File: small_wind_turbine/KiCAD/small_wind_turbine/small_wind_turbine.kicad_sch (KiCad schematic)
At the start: 17 parts

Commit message: wip schematic
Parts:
- added R? (x2): 2.5k, symbol Device:R
- added R?: 100, symbol Device:R
- added U? (x5): Opamp_Quad, symbol Device:Opamp_Quad
- added U?: AD8276, symbol Amplifier_Difference:AD8276
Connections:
- net GND1: now also U?.1 (REF), U?.11 (V-), U?.4 (V-), U?.9 (-)
- net OUTPUT_ISENSE_DOWNSTREAM: now reaches J?.1 (Pin_1), R?.2
- net OUTPUT_ISENSE_DOWNSTREAM: now also U?.5 (+)
- net RECTIFIER_VDD renamed OUTPUT_ISENSE_UPSTREAM
- net OUTPUT_ISENSE_UPSTREAM: now also U?.3 (+)
- new net: R?.1, R?.2, R?.2, U?.10 (+)
- new net: R?.1, U?.5 (SENSE), U?.6
- new net: U?.2 (-), U?.6 (-), U?.7
- new net: U?.1, U?.2 (-), U?.3 (+)
- new net: R?.2, U?.8
- new net +5V: U?.4 (V+), U?.7 (V+)
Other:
- moved on the sheet: U?

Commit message: finish current sensing feedback circuit
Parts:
- added C? (x3): C, symbol Device:C
- added R? (x3): R, symbol Device:R
- added U?: MCP3021, symbol just_energy_hub:MCP3021
- added U?: MCP4725xxx-xCH, Package_TO_SOT_SMD:SOT-23-6, symbol Analog_DAC:MCP4725xxx-xCH
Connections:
- net OUTPUT_ISENSE_DOWNSTREAM is gone; now on net BATTERY_POSITIVE: J?.1 (Pin_1), R?.2, U?.5 (+)
- net +5V: now also U?.1 (VDD), U?.3 (VDD)
- net GND1: now also C?.2, U?.2 (VSS), U?.2 (VSS)
- net at R?.1: now also U?.1 (VOUT)
- net UC2844_COMP: now reaches U?.1 (COMP)
- net UC2844_COMP: now also C?.1, C?.2
- net UC2844_FB: now reaches U?.2 (FB)
- net UC2844_FB: now also C?.2, R?.1, R?.2
- net UC2844_ISENSE: now reaches U?.3 (ISENSE)
- net UC2844_ISENSE: now also Q?.1 (D), R?.2
- net UC2844_RTCT: now reaches U?.4 (RT/CT)
- net UC2844_RTCT: now also C?.1, R?.2
- net UC2844_GATE_DRIVE: now reaches U?.6 (OUTPUT)
- net UC2844_GATE_DRIVE: now also Q?.2 (G)
- net UC2844_VREF: now reaches U?.8 (VREF)
- net UC2844_VREF: now also R?.1
- net BATTERY_NEGATIVE: now reaches C?.2, J?.2 (Pin_2), L?.1
- net BATTERY_POSITIVE: now reaches U?.12 (+)
- net at U?.13 (-): now also U?.14, U?.3 (AIN)
- net at R?.2, U?.8: now also R?.1
- new net: C?.1, R?.2
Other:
- moved on the sheet: C?, D?, J?, L?, Q?, R?, U?, U?A, U?B, U?C, U?E

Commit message: wip schematic
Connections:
- net GND: now also U?.5 (GND)
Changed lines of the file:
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@@
     (stroke (width 0) (type default) (color 0 0 0 0))
   )
-  (wire (pts (xy 41.91 195.58) (xy 41.91 201.93))
+  (wire (pts (xy 41.91 195.58) (xy 41.91 198.12))
     (stroke (width 0) (type default) (color 0 0 0 0))
   )
@@
   (label "UC2844_RTCT" (at 45.72 149.86 180)
     (effects (font (size 1.27 1.27)) (justify right bottom))
+  )
+  (label "RECTIFIER_GND" (at 68.58 149.86 0)
+    (effects (font (size 1.27 1.27)) (justify left bottom))
   )
   (label "OUTPUT_ISENSE_DOWNSTREAM" (at 121.92 71.12 0)
@@
     (pin "2")
   )
-  (symbol (lib_id "power:GND1") (at 41.91 201.93 0) (unit 1)
+  (symbol (lib_id "power:GND1") (at 41.91 198.12 0) (unit 1)
     (in_bom yes) (on_board yes) (fields_autoplaced)
-    (property "Reference" "#PWR?" (id 0) (at 41.91 208.28 0)
+    (property "Reference" "#PWR?" (id 0) (at 41.91 204.47 0)
       (effects (font (size 1.27 1.27)) hide)
     )
-    (property "Value" "GND1" (id 1) (at 41.91 207.01 0))
-    (property "Footprint" "" (id 2) (at 41.91 201.93 0)
+    (property "Value" "GND1" (id 1) (at 41.91 203.2 0))
+    (property "Footprint" "" (id 2) (at 41.91 198.12 0)
       (effects (font (size 1.27 1.27)) hide)
     )
-    (property "Datasheet" "" (id 3) (at 41.91 201.93 0)
+    (property "Datasheet" "" (id 3) (at 41.91 198.12 0)
       (effects (font (size 1.27 1.27)) hide)
     )

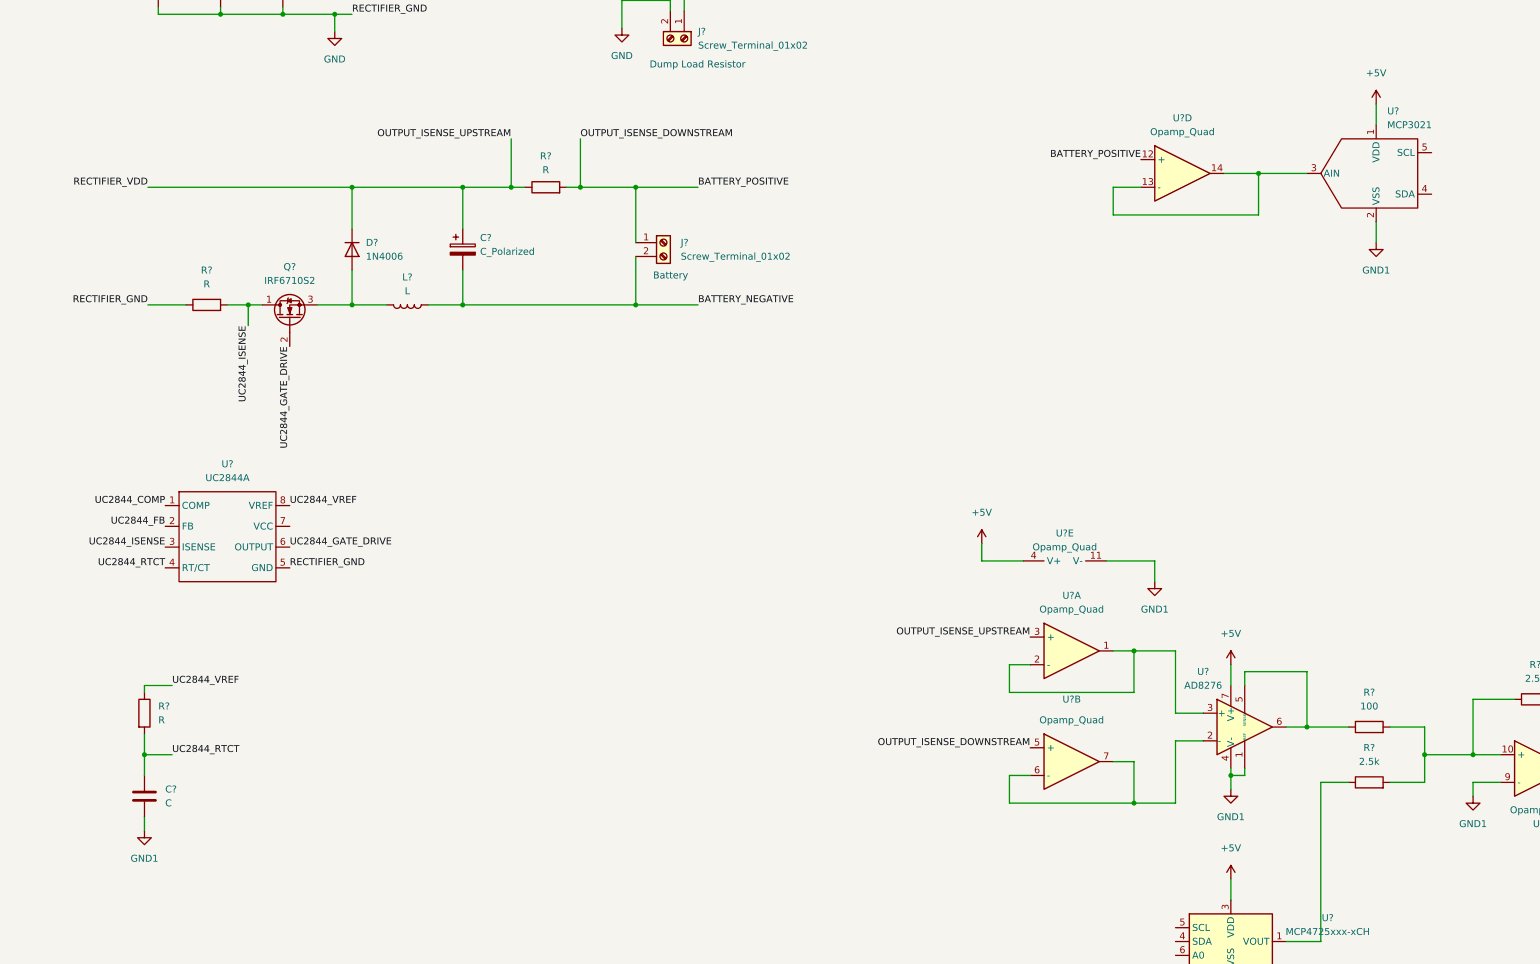
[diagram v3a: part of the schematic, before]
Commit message: add high side gate driver and connect common grounds
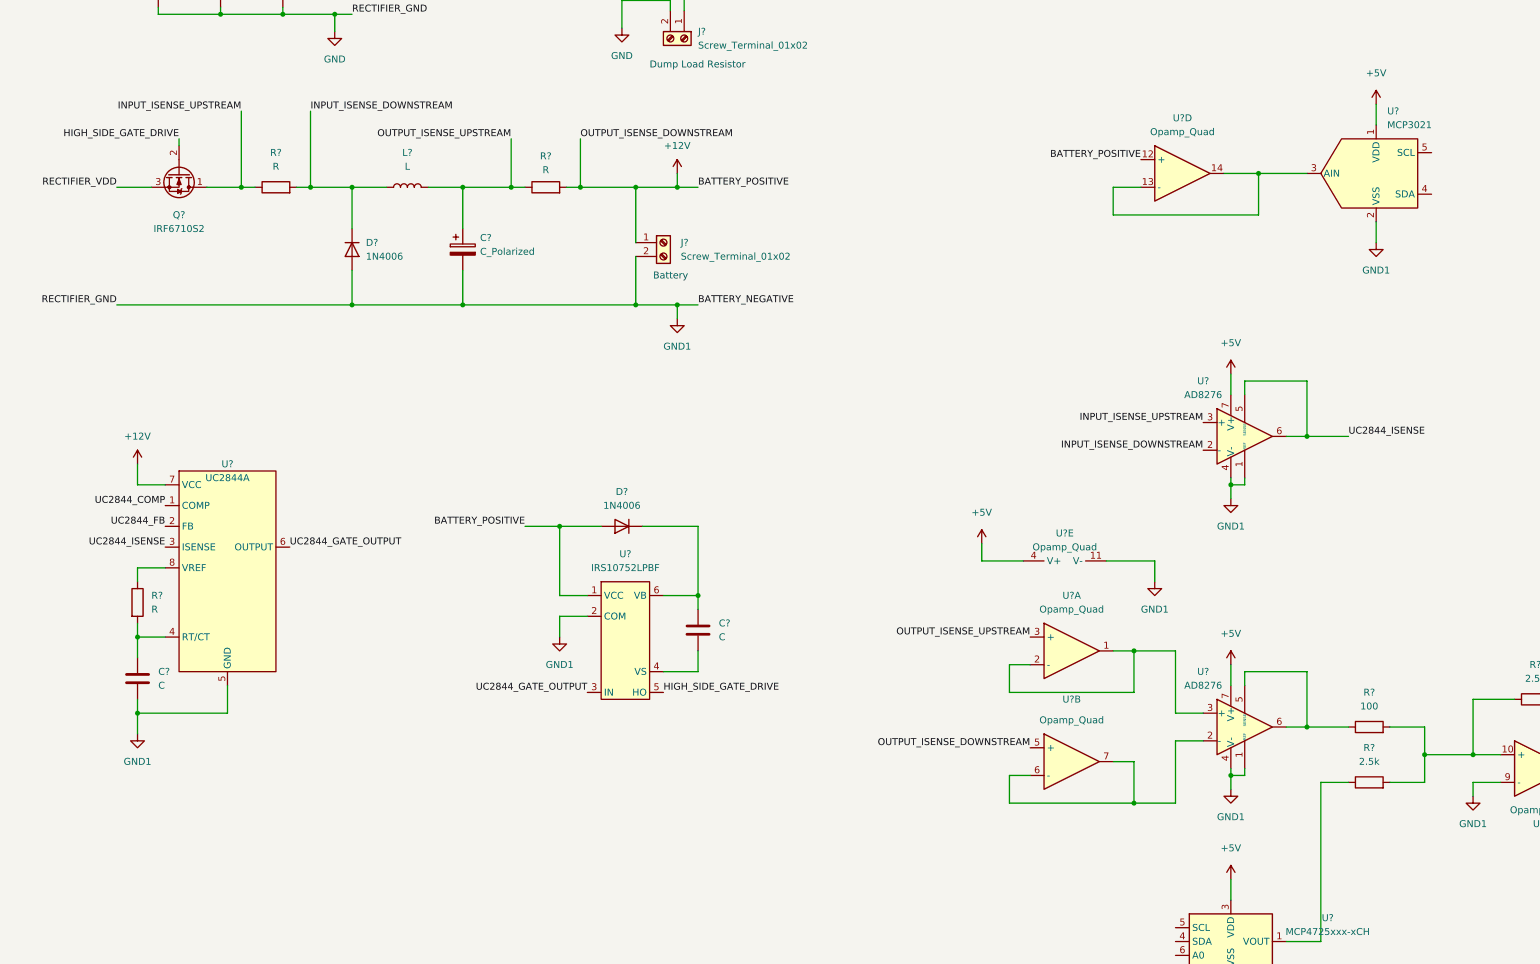
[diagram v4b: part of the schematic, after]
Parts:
- added C?: C, symbol Device:C
- added D?: 1N4006, Diode_THT:D_DO-41_SOD81_P10.16mm_Horizontal, symbol Diode:1N4006
- added U?: IRS10752LPBF, symbol just_energy_hub:IRS10752LPBF
- added U?: AD8276, symbol Amplifier_Difference:AD8276
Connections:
- net BATTERY_POSITIVE is gone; now on net +12V: J?.1 (Pin_1), R?.2, U?.12 (+), U?.5 (+)
- net GND1 is gone; now on net GND: C?.2, K?.A1, U?.1 (REF), U?.11 (V-), U?.2 (VSS), U?.2 (VSS), U?.4 (V-), U?.9 (-)
- net +5V: now also U?.7 (V+)
- net GND: now also C?.2, D?.2 (A), J?.2 (Pin_2), U?.1 (REF), U?.2 (COM), U?.4 (V-); no longer R?.1
- net OUTPUT_ISENSE_UPSTREAM: now also L?.2; no longer D?.1 (K), SW?.1 (A)
- net UC2844_ISENSE: now also U?.5 (SENSE), U?.6; no longer Q?.1 (D), R?.2
- net +12V: now reaches U?.7 (VCC)
- net +12V: now also D?.2 (A), U?.1 (VCC)
- removed net BATTERY_NEGATIVE: C?.2, J?.2 (Pin_2), L?.1
- net UC2844_GATE_DRIVE renamed HIGH_SIDE_GATE_DRIVE
- net HIGH_SIDE_GATE_DRIVE: now also U?.5 (HO); no longer U?.6 (OUTPUT)
- net UC2844_RTCT: no longer names the net of C?.1, R?.2, U?.4 (RT/CT)
- net UC2844_VREF: no longer names the net of R?.1, U?.8 (VREF)
- new net: C?.2, U?.4 (VS)
- new net: C?.1, D?.1 (K), U?.6 (VB)
- new net INPUT_ISENSE_DOWNSTREAM: D?.1 (K), L?.1, R?.2, U?.2 (-)
- new net INPUT_ISENSE_UPSTREAM: Q?.1 (D), R?.1, U?.3 (+)
- new net RECTIFIER_VDD: Q?.3 (S), SW?.1 (A)
- new net UC2844_GATE_OUTPUT: U?.3 (IN), U?.6 (OUTPUT)
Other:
- moved on the sheet: C?, L?, Q?, R?

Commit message: wip schematic. Replace inverting adder with non-inverting adder. Postulate on replacing Isense resistor for UC2844
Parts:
- added D?: D_Zener, symbol Device:D_Zener
- added J?: Screw_Terminal_01x03, symbol Connector:Screw_Terminal_01x03
- added R?: 100, symbol Device:R
- added R? (x2): 4.7k, symbol Device:R
- added R?: 62k, symbol Device:R
- added R?: 10k, symbol Device:R
- added U?: AZ1117-5.0, symbol Regulator_Linear:AZ1117-5.0
- added U?: WeMos_D1_mini, Module:WEMOS_D1_mini_light, symbol MCU_Module:WeMos_D1_mini
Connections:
- net +12V: now also U?.2 (-), R?.1, U?.3 (VI); no longer U?.12 (+), U?.5 (+)
- net +5V: now also U?.11 (V-), U?.6 (A0); no longer U?.4 (V+)
- net GND: now also U?.4 (V+), D?.2 (A), R?.2, R?.2, U?.1 (GND), U?.10 (GND); no longer U?.11 (V-), U?.9 (-)
- net OUTPUT_ISENSE_UPSTREAM: now also U?.3 (+); no longer U?.3 (+)
- net RELAY_DRIVE: now also U?.3 (D0)
- net UC2844_ISENSE: now also R?.2, U?.5 (SENSE), U?.6
- net at R?.1: now also R?.1, U?.10 (+); no longer U?.1 (VOUT)
- net at U?.13 (-), U?.14, U?.3 (AIN): now also D?.1 (K)
- net WEMOS_SDA: now reaches U?.4 (SDA)
- net WEMOS_SDA: now also U?.4 (SDA), R?.2, U?.13 (SDA/D2)
- net WEMOS_SCL: now reaches U?.5 (SCL)
- net WEMOS_SCL: now also U?.5 (SCL), R?.2, U?.14 (SCL/D1)
- net PHASE_1_IN: no longer names the net of D?.1 (K), D?.2 (A)
- net PHASE_1_IN: now also J?.3 (Pin_3)
- net PHASE_2_IN: no longer names the net of D?.1 (K), D?.2 (A)
- net PHASE_2_IN: now also J?.2 (Pin_2)
- net PHASE_3_IN: no longer names the net of D?.1 (K), D?.2 (A)
- net PHASE_3_IN: now also J?.1 (Pin_1)
- new net: R?.2, U?.1 (VOUT)
- new net: U?.2 (VO), U?.9 (5V)
- new net: R?.1, R?.1, U?.9 (-)
- new net: R?.1, R?.2, U?.12 (+)
- new net +3V3: R?.1, R?.1, U?.8 (3V3)
- now unconnected: U?.1, U?.2 (-), U?.6 (-), U?.7
- no-connect marks 0 -> 10
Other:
- note added: "14.4V"
- note added: "2V"
- note added: "3 Phase In"
- note added: "3.3V For Protection"
- note added: "DELETE Use OUTPUT_ISENSE_DOWNSTREAM Instead"
- note added: "I Think"
- moved on the sheet: D?, R?, U?, U?A, U?B, U?E

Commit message: tidy KiCAD schematic
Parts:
- added R?: 4.7k, symbol Device:R
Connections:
- net +5V: now also U?.2 (VO), U?.9 (5V)
- net GND: now also R?.2
- net INPUT_ISENSE_DOWNSTREAM: now also C?.1, R?.1, U?.3 (+); no longer D?.1 (K), L?.1
- net INPUT_ISENSE_UPSTREAM: now also L?.2; no longer Q?.1 (D)
- net RELAY_DRIVE: now also R?.1
- net UC2844_ISENSE: no longer R?.2, U?.5 (SENSE), U?.6
- removed net OUTPUT_ISENSE_UPSTREAM: C?.1, L?.2, R?.1, U?.3 (+)
- new net: R?.2, U?.5 (SENSE), U?.6
- new net: D?.1 (K), L?.1, Q?.1 (D)
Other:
- note added: "Battery Voltage Monitor"
- note added: "Bootstrap Gate Driver"
- note added: "Buck Converter"
- note added: "Compensator"
- note added: "Generator Rectifier and Disconnect"
- note added: "UC2844"
- note added: "UC2844 Isense Connection"
- note added: "WeMos D1 Mini"
- note removed: "DELETE Use OUTPUT_ISENSE_DOWNSTREAM Instead"
- note removed: "I Think"
- moved on the sheet: C?, D?, J?, K?, L?, Q?, R?, SW?, U?, U?A, U?B, U?C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

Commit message: clean up and annotate schematic
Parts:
- added R2: 9k, symbol Device:R
- added R3: 1k, symbol Device:R
- Cbuck1: renamed from C?; value C_Polarized -> 200u
- Cc1: renamed from C?; value C -> 470n
- Cc2: renamed from C?; value C -> 33n
- Ct1: renamed from C?; value C -> 2.2n
- Lbuck1: renamed from L?; value L -> 345u
- R7, R8: renamed from R?; value 2.5k -> 1k
- Rc1: renamed from R?; value R -> 255
- Rf1: renamed from R?; value R -> 5.1k
- Rsh1, Rsh2: renamed from R?; value R -> 50m
- Rt1: renamed from R?; value R -> 7.87k
- gave numbers to parts that had none: 32
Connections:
- net INPUT_ISENSE_DOWNSTREAM is gone; now on net +12V: Cbuck1.1, Rsh1.2, Rsh2.1, U5.2 (-), U6.3 (+)
- net +12V: no longer Jbat1.1 (Pin_1), R4.1, Rsh2.2, U6.2 (-)
- net GND: now also R3.2
- net at U6.5 (SENSE), U6.6: now also U4.3 (+); no longer R6.2
- net at U4.5 (+): now also U4.1, R2.1
- net at U4.6 (-): now also R6.2, U4.7
- net at U4.2 (-): now also R2.2, R3.1
- new net BATTERY_POSITIVE: Jbat1.1 (Pin_1), R4.1, Rsh2.2, U6.2 (-)
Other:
- note added: "WHERE DO THE BUFFERS NEED TO GO?"
- moved on the sheet: R6, U4A, U4B, U6, U8

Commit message: add gate resistor and source connection to gate driver
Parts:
- added R?: 75, symbol Device:R
- Cbs1: value C -> 10u
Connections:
- net HIGH_SIDE_GATE_DRIVE: now also R?.2; no longer U3.5 (HO)
- net GATE_SOURCE: now reaches Cbs1.2, U3.4 (VS)
- net GATE_SOURCE: now also Dbuck1.1 (K), Lbuck1.1, Qbuck1.1 (D)
- new net: R?.1, U3.5 (HO)
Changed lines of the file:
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@@
   (junction (at 111.76 123.19) (diameter 0) (color 0 0 0 0)
   )
+  (junction (at 153.67 257.81) (diameter 0) (color 0 0 0 0)
+  )
   (junction (at 73.025 41.91) (diameter 0) (color 0 0 0 0)
   )
@@
   )
   (junction (at 128.27 231.14) (diameter 0) (color 0 0 0 0)
+  )
+  (junction (at 64.77 101.6) (diameter 0) (color 0 0 0 0)
   )
   (no_connect (at 367.03 44.45))
@@
     (stroke (width 0) (type default) (color 0 0 0 0))
   )
-  (polyline (pts (xy 186.69 234.95) (xy 186.69 191.77))
+  (polyline (pts (xy 193.04 234.95) (xy 193.04 191.77))
     (stroke (width 0) (type default) (color 0 0 0 0))
   )
@@
     (stroke (width 0) (type default) (color 0 0 0 0))
   )
-  (polyline (pts (xy 97.79 274.32) (xy 179.07 274.32))
+  (polyline (pts (xy 97.79 274.32) (xy 189.23 274.32))
     (stroke (width 0) (type default) (color 0 0 0 0))
   )
@@
     (stroke (width 0) (type default) (color 0 0 0 0))
   )
-  (wire (pts (xy 57.15 92.71) (xy 57.15 93.98))
+  (wire (pts (xy 57.15 86.36) (xy 57.15 93.98))
     (stroke (width 0) (type default) (color 0 0 0 0))
   )
@@
     (stroke (width 0) (type default) (color 0 0 0 0))
   )
-  (polyline (pts (xy 398.78 234.95) (xy 186.69 234.95))
+  (polyline (pts (xy 398.78 234.95) (xy 193.04 234.95))
     (stroke (width 0) (type default) (color 0 0 0 0))
   )
@@
     (stroke (width 0) (type default) (color 0 0 0 0))
   )
+  (wire (pts (xy 64.77 101.6) (xy 62.23 101.6))
+    (stroke (width 0) (type default) (color 0 0 0 0))
+  )
   (wire (pts (xy 355.6 40.64) (xy 355.6 44.45))
     (stroke (width 0) (type default) (color 0 0 0 0))
@@
     (stroke (width 0) (type default) (color 0 0 0 0))
   )
-  (polyline (pts (xy 179.07 219.71) (xy 97.79 219.71))
-    (stroke (width 0) (type default) (color 0 0 0 0))
-  )
-  (wire (pts (xy 68.58 101.6) (xy 62.23 101.6))
+  (wire (pts (xy 64.77 86.36) (xy 64.77 101.6))
+    (stroke (width 0) (type default) (color 0 0 0 0))
+  )
+  (wire (pts (xy 153.67 257.81) (xy 165.1 257.81))
+    (stroke (width 0) (type default) (color 0 0 0 0))
+  )
+  (polyline (pts (xy 189.23 219.71) (xy 97.79 219.71))
+    (stroke (width 0) (type default) (color 0 0 0 0))
+  )
+  (wire (pts (xy 68.58 101.6) (xy 64.77 101.6))
     (stroke (width 0) (type default) (color 0 0 0 0))
   )
@@
     (stroke (width 0) (type default) (color 0 0 0 0))
   )
-  (polyline (pts (xy 186.69 191.77) (xy 130.81 191.77))
+  (polyline (pts (xy 193.04 191.77) (xy 130.81 191.77))
     (stroke (width 0) (type default) (color 0 0 0 0))
   )
@@
     (stroke (width 0) (type default) (color 0 0 0 0))
   )
-  (polyline (pts (xy 179.07 274.32) (xy 179.07 219.71))
+  (wire (pts (xy 147.32 261.62) (xy 152.4 261.62))
+    (stroke (width 0) (type default) (color 0 0 0 0))
+  )
+  (polyline (pts (xy 189.23 274.32) (xy 189.23 219.71))
     (stroke (width 0) (type default) (color 0 0 0 0))
   )
@@
   )
   (wire (pts (xy 306.07 186.69) (xy 314.96 186.69))
+    (stroke (width 0) (type default) (color 0 0 0 0))
+  )
+  (wire (pts (xy 160.02 261.62) (xy 165.1 261.62))
     (stroke (width 0) (type default) (color 0 0 0 0))
   )
@@
     (effects (font (size 1.27 1.27)) (justify right bottom))
   )
-  (label "HIGH_SIDE_GATE_DRIVE" (at 147.32 261.62 0)
+  (label "HIGH_SIDE_GATE_DRIVE" (at 165.1 261.62 0)
     (effects (font (size 1.27 1.27)) (justify left bottom))
   )
@@
     (effects (font (size 1.27 1.27)) (justify left bottom))
   )
+  (label "GATE_SOURCE" (at 165.1 257.81 0)
+    (effects (font (size 1.27 1.27)) (justify left bottom))
+  )
   (label "INPUT_ISENSE_UPSTREAM" (at 48.26 243.84 180)
     (effects (font (size 1.27 1.27)) (justify right bottom))
   )
-  (label "HIGH_SIDE_GATE_DRIVE" (at 57.15 92.71 180)
+  (label "HIGH_SIDE_GATE_DRIVE" (at 57.15 86.36 180)
     (effects (font (size 1.27 1.27)) (justify right bottom))
   )
   (label "INPUT_ISENSE_UPSTREAM" (at 91.44 92.71 180)
     (effects (font (size 1.27 1.27)) (justify right bottom))
+  )
+  (label "GATE_SOURCE" (at 64.77 86.36 0)
+    (effects (font (size 1.27 1.27)) (justify left bottom))
   )
   (label "WEMOS_SCL" (at 382.27 110.49 270)
@@
     (pin "1")
   )
+  (symbol (lib_id "Device:R") (at 156.21 261.62 90) (unit 1)
+    (in_bom yes) (on_board yes)
+    (property "Reference" "R?" (id 0) (at 156.21 266.7 90))
+    (property "Value" "75" (id 1) (at 156.21 264.16 90))
+    (property "Footprint" "" (id 2) (at 156.21 263.398 90)
+      (effects (font (size 1.27 1.27)) hide)
+    )
+    (property "Datasheet" "~" (id 3) (at 156.21 261.62 0)
+      (effects (font (size 1.27 1.27)) hide)
+    )
+    (pin "1")
+    (pin "2")
+  )
   (symbol (lib_id "Device:C") (at 36.83 196.85 0) (unit 1)
     (in_bom yes) (on_board yes)
@@
       (effects (font (size 1.27 1.27)) (justify left))
     )
-    (property "Value" "C" (id 1) (at 157.48 251.4599 0)
+    (property "Value" "10u" (id 1) (at 157.48 251.4599 0)
       (effects (font (size 1.27 1.27)) (justify left))
     )
@@
     )
     (path "/fab904b1-71c8-463b-9d93-e03e494df6c7"
-      (reference "Cbs1") (unit 1) (value "C") (footprint "")
+      (reference "Cbs1") (unit 1) (value "10u") (footprint "")
     )
     (path "/ce1db8e6-3d8b-4bfe-86e5-0de534ab5768"
@@
       (reference "R11") (unit 1) (value "4.7k") (footprint "")
     )
+    (path "/f55259eb-0b9c-423b-a8a7-e93dd66e654e"
+      (reference "R?") (unit 1) (value "75") (footprint "")
+    )
     (path "/3b27ad75-5331-404a-ba3f-3b8ff7fd549f"
